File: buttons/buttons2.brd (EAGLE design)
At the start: 72 x 44 mm, 14 parts, among them U1 attiny2313

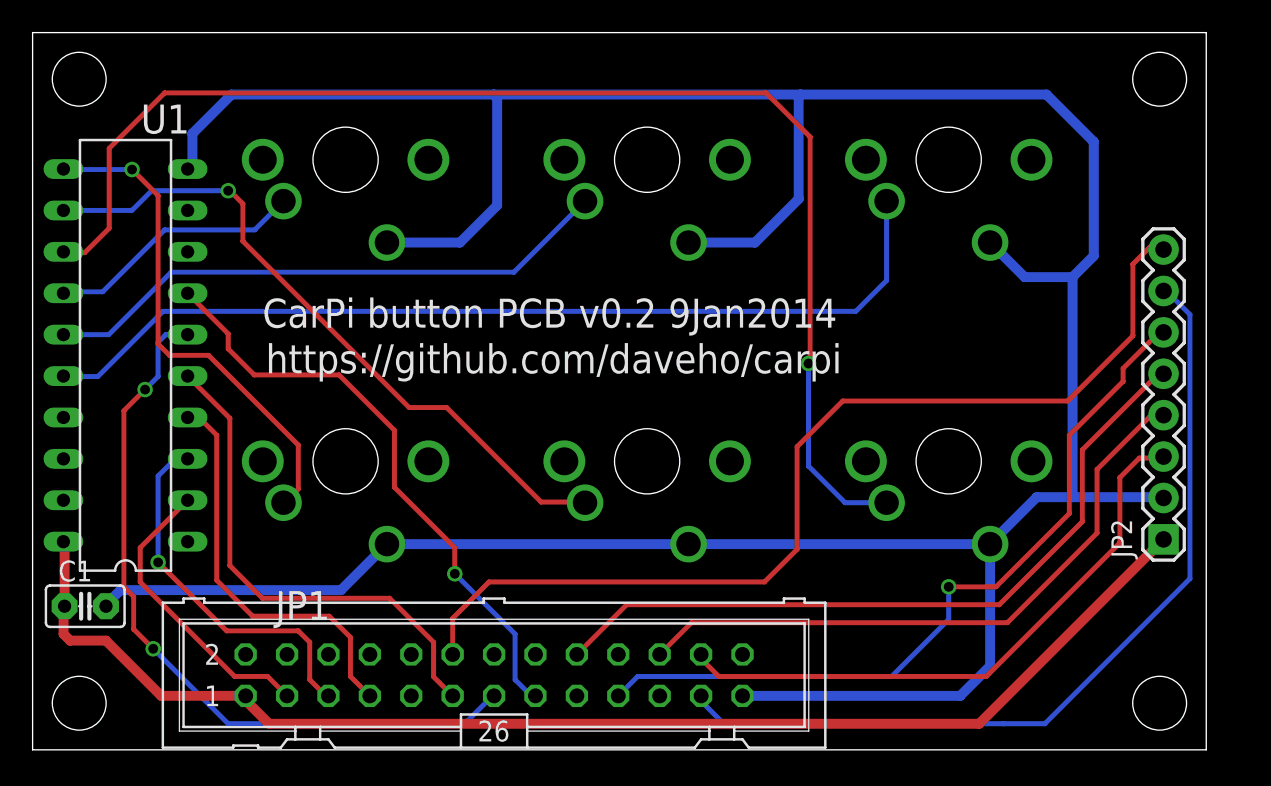
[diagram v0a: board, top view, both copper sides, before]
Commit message: making everything fit for Cherry MX keyswitches
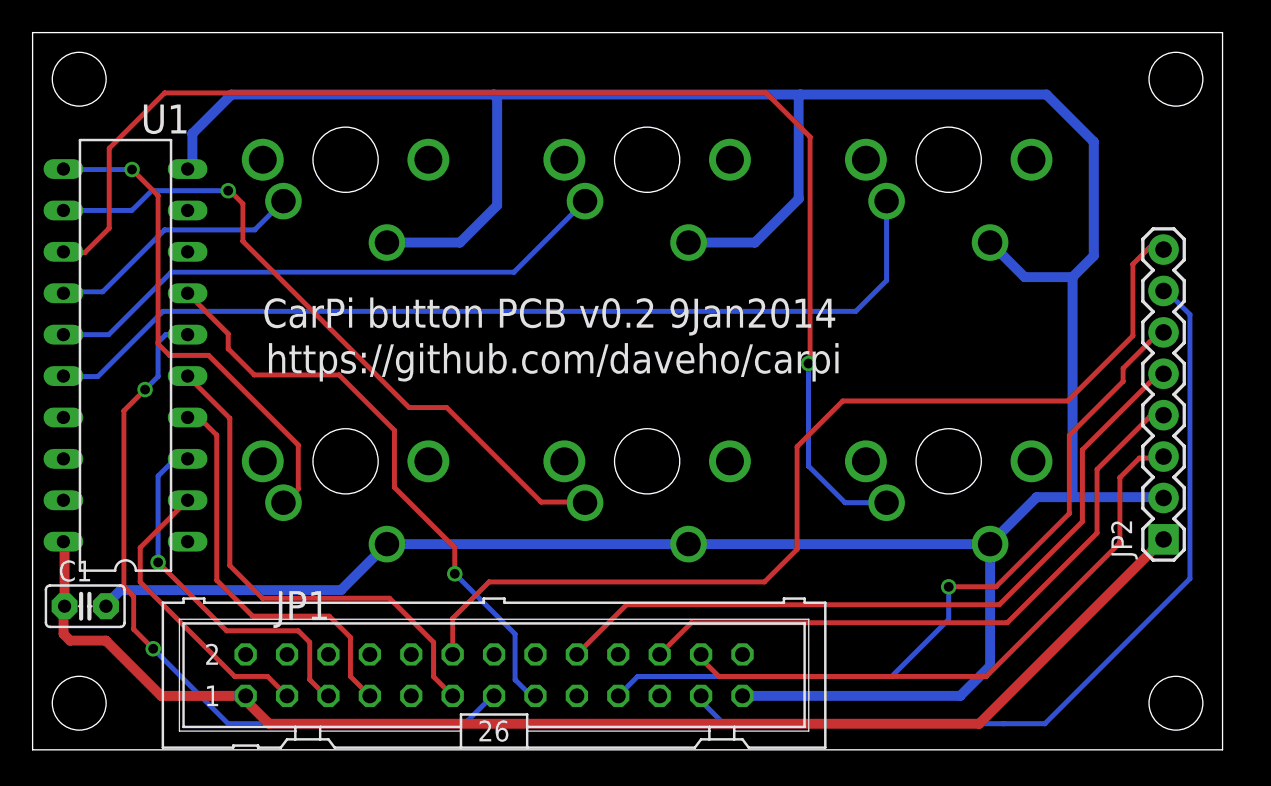
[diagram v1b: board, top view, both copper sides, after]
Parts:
- moved STANDOFF1 1.00 mm to (70.1, 2.86)
- moved STANDOFF3 1.00 mm to (70.1, 41.1)
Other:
- board size 72 x 44 mm -> 73 x 44 mm
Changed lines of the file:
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@@
 <board>
 <plain>
-<wire x1="0" y1="0" x2="72" y2="0" width="0" layer="20"/>
-<wire x1="72" y1="0" x2="72" y2="44" width="0" layer="20"/>
-<wire x1="72" y1="44" x2="0" y2="44" width="0" layer="20"/>
+<wire x1="0" y1="0" x2="73" y2="0" width="0" layer="20"/>
+<wire x1="73" y1="0" x2="73" y2="44" width="0" layer="20"/>
+<wire x1="73" y1="44" x2="0" y2="44" width="0" layer="20"/>
 <wire x1="0" y1="44" x2="0" y2="0" width="0" layer="20"/>
 <text x="14.1" y="25.9" size="1.778" layer="21" font="vector">CarPi button PCB v0.2 9Jan2014</text>
@@
 <attribute name="VALUE" x="0.679" y="6.016" size="1.27" layer="27" font="vector" ratio="10"/>
 </element>
-<element name="STANDOFF1" library="SparkFun-Electromechanical" package="STAND-OFF" value="STAND-OFF" x="69.14" y="2.86"/>
+<element name="STANDOFF1" library="SparkFun-Electromechanical" package="STAND-OFF" value="STAND-OFF" x="70.14" y="2.86"/>
 <element name="STANDOFF2" library="SparkFun-Electromechanical" package="STAND-OFF" value="STAND-OFF" x="2.86" y="2.86"/>
-<element name="STANDOFF3" library="SparkFun-Electromechanical" package="STAND-OFF" value="STAND-OFF" x="69.14" y="41.14"/>
+<element name="STANDOFF3" library="SparkFun-Electromechanical" package="STAND-OFF" value="STAND-OFF" x="70.14" y="41.14"/>
 <element name="STANDOFF4" library="SparkFun-Electromechanical" package="STAND-OFF" value="STAND-OFF" x="2.86" y="41.14"/>
 <element name="S1" library="cherrymx" package="CHERRY-MX-I" value="CHERRY-MX-I" x="19.2" y="17.7" rot="MR180"/>

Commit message: allow 19mm H/V between switch centers
The keycaps are 18mm x 18mm, so hopefull this is enough
room.
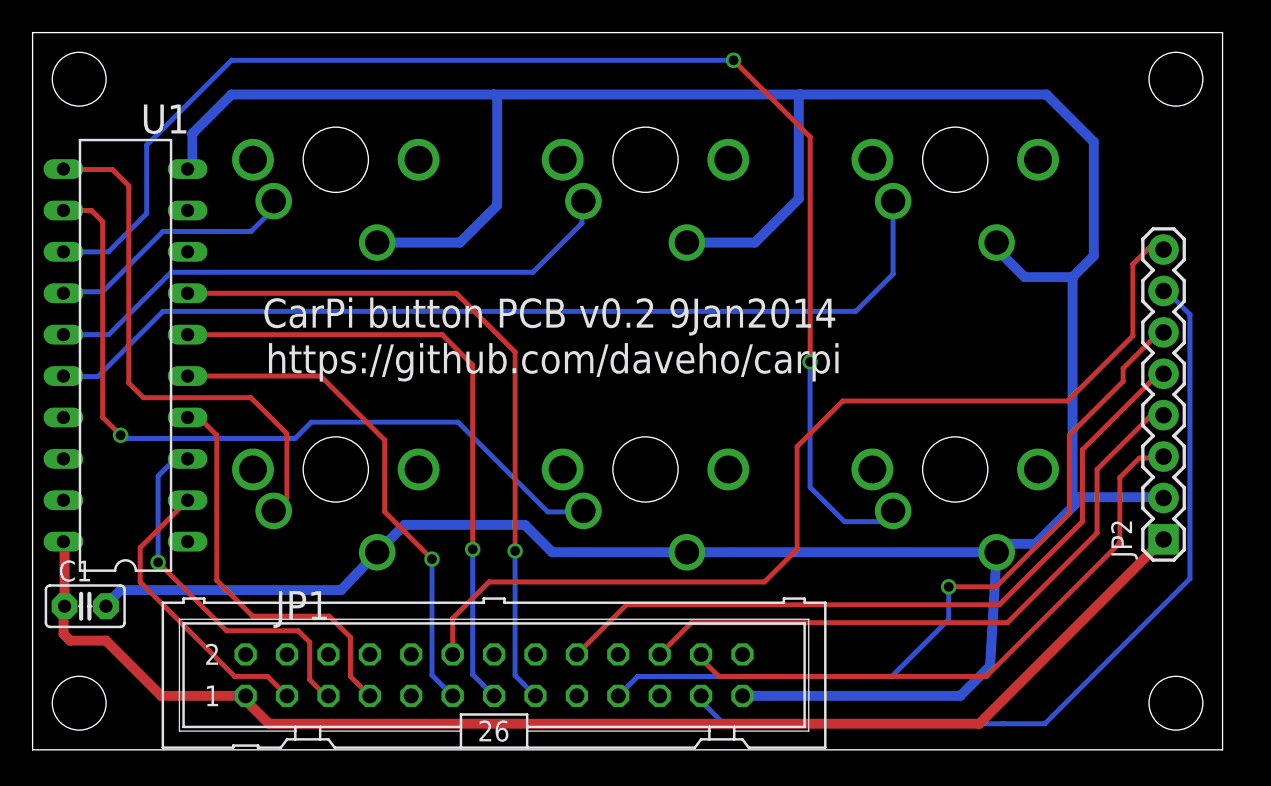
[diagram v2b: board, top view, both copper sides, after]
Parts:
- moved S1 0.78 mm to (18.6, 17.2)
- moved S3 0.64 mm to (56.6, 17.2)
- moved S4 0.60 mm to (18.6, 36.2)
- moved S2 0.51 mm to (37.6, 17.2)
- moved S6 0.40 mm to (56.6, 36.2)
- moved S5 0.10 mm to (37.6, 36.2)
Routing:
- net BUTTON5: track 45.9 -> 39.1 mm, vias 2 -> 1
- net BUTTON6: track 36.7 -> 43.2 mm
- net N$5: track 42.0 -> 47.4 mm
- net N$4: track 79.7 -> 82.8 mm, vias 1 -> 2
- net GND: track 208.3 -> 211.4 mm
- net N$6: track 30.7 -> 32.6 mm, vias 1 -> 0
- net N$2: track 35.4 -> 36.0 mm
- net BUTTON4: track 30.9 -> 31.1 mm, vias 0 -> 1

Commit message: various layout tweaks, improved clearances, etc.
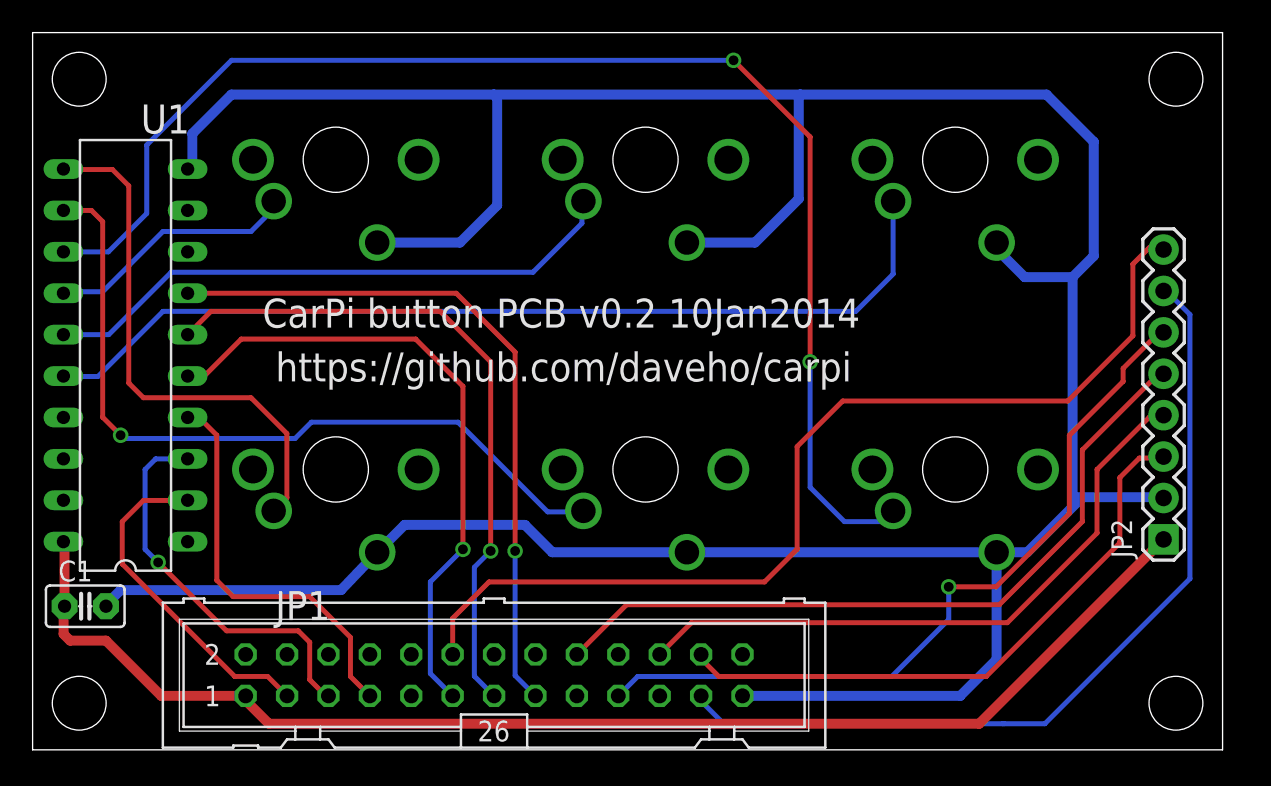
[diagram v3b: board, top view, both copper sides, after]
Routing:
- net BUTTON4: track 31.1 -> 39.4 mm
- net BUTTON5: track 39.1 -> 41.9 mm
- net BUTTON1: track 18.1 -> 20.6 mm
- net BUTTON2: track 22.7 -> 24.1 mm
- net GND: track 211.4 -> 210.7 mm
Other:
- board text added: "CarPi button PCB v0.2 10Jan2014"
- board text removed: "CarPi button PCB v0.2 9Jan2014"
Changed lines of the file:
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@@
 <wire x1="73" y1="44" x2="0" y2="44" width="0" layer="20"/>
 <wire x1="0" y1="44" x2="0" y2="0" width="0" layer="20"/>
-<text x="14.1" y="25.9" size="1.778" layer="21" font="vector">CarPi button PCB v0.2 9Jan2014</text>
-<text x="14.3" y="23.1" size="1.778" layer="21" font="vector">https://github.com/daveho/carpi</text>
+<text x="14.1" y="25.9" size="1.778" layer="21" font="vector">CarPi button PCB v0.2 10Jan2014</text>
+<text x="14.9" y="22.6" size="1.778" layer="21" font="vector">https://github.com/daveho/carpi</text>
 </plain>
 <attributes>
@@
 <contactref element="U1" pad="10"/>
 <contactref element="U1" pad="10"/>
-<wire x1="58.74" y1="5.14" x2="59.14" y2="12.12" width="0.6096" layer="16"/>
-<wire x1="59.14" y1="12.12" x2="58.74" y2="12.64" width="0.6096" layer="16"/>
 <wire x1="63.8" y1="15.5" x2="64.4" y2="15.5" width="0.6096" layer="16"/>
 <wire x1="64.4" y1="15.5" x2="69.33" y2="15.5" width="0.6096" layer="16"/>
@@
 <wire x1="9.8" y1="37.8" x2="12.2" y2="40.2" width="0.6096" layer="16"/>
 <wire x1="43.55" y1="3.31" x2="56.91" y2="3.31" width="0.6096" layer="16"/>
-<wire x1="56.91" y1="3.31" x2="58.74" y2="5.14" width="0.6096" layer="16"/>
+<wire x1="56.91" y1="3.31" x2="59.14" y2="5.54" width="0.6096" layer="16"/>
 <wire x1="12.2" y1="40.2" x2="28.3" y2="40.2" width="0.6096" layer="16"/>
 <wire x1="28.3" y1="40.2" x2="47.1" y2="40.2" width="0.6096" layer="16"/>
@@
 <wire x1="28.5" y1="33.4" x2="28.5" y2="40" width="0.6096" layer="16"/>
 <wire x1="28.5" y1="40" x2="28.3" y2="40.2" width="0.6096" layer="16"/>
-<wire x1="58.74" y1="12.64" x2="61.54" y2="12.64" width="0.6096" layer="16"/>
-<wire x1="61.54" y1="12.64" x2="64.4" y2="15.5" width="0.6096" layer="16"/>
+<wire x1="61.02" y1="12.12" x2="64.4" y2="15.5" width="0.6096" layer="16"/>
 <wire x1="59.14" y1="31.12" x2="58.94" y2="30.92" width="0.6096" layer="16"/>
 <wire x1="58.94" y1="30.92" x2="60.86" y2="29" width="0.6096" layer="16"/>
@@
 <wire x1="30.2" y1="13.8" x2="31.88" y2="12.12" width="0.6096" layer="16"/>
 <wire x1="31.88" y1="12.12" x2="40.14" y2="12.12" width="0.6096" layer="16"/>
+<wire x1="59.14" y1="12.12" x2="59.14" y2="5.54" width="0.6096" layer="16"/>
+<wire x1="59.14" y1="12.12" x2="61.02" y2="12.12" width="0.6096" layer="16"/>
 </signal>
 <signal name="N$1">
@@
 <contactref element="U1" pad="2"/>
 <wire x1="15.61" y1="3.31" x2="14.42" y2="4.5" width="0.3048" layer="1"/>
-<wire x1="6.6" y1="12.4" x2="9.51" y2="15.31" width="0.3048" layer="1"/>
-<wire x1="6.6" y1="12.4" x2="6.6" y2="10.3" width="0.3048" layer="1"/>
-<wire x1="6.6" y1="10.3" x2="12.4" y2="4.5" width="0.3048" layer="1"/>
+<wire x1="5.5" y1="11.4" x2="12.4" y2="4.5" width="0.3048" layer="1"/>
 <wire x1="12.4" y1="4.5" x2="14.42" y2="4.5" width="0.3048" layer="1"/>
+<wire x1="5.5" y1="11.4" x2="5.5" y2="14" width="0.3048" layer="1"/>
+<wire x1="5.5" y1="14" x2="6.8" y2="15.3" width="0.3048" layer="1"/>
+<wire x1="6.8" y1="15.3" x2="9.5" y2="15.3" width="0.3048" layer="1"/>
+<wire x1="9.5" y1="15.3" x2="9.51" y2="15.31" width="0.3048" layer="1"/>
 </signal>
 <signal name="BUTTON2">
@@
 <wire x1="11.9" y1="7.3" x2="7.7" y2="11.5" width="0.3048" layer="1"/>
 <via x="7.7" y="11.5" extent="1-16" drill="0.6"/>
-<wire x1="7.7" y1="11.5" x2="7.7" y2="16.8" width="0.3048" layer="16"/>
-<wire x1="7.7" y1="16.8" x2="8.7" y2="17.8" width="0.3048" layer="16"/>
-<wire x1="8.7" y1="17.8" x2="9.46" y2="17.8" width="0.3048" layer="16"/>
-<wire x1="9.46" y1="17.8" x2="9.51" y2="17.85" width="0.3048" layer="16"/>
+<wire x1="9.51" y1="17.85" x2="7.55" y2="17.85" width="0.3048" layer="16"/>
+<wire x1="7.55" y1="17.85" x2="6.9" y2="17.2" width="0.3048" layer="16"/>
+<wire x1="6.9" y1="17.2" x2="6.9" y2="12.3" width="0.3048" layer="16"/>
+<wire x1="6.9" y1="12.3" x2="7.7" y2="11.5" width="0.3048" layer="16"/>
 </signal>
 <signal name="BUTTON3">
@@
 <wire x1="20.69" y1="3.31" x2="19.5" y2="4.5" width="0.3048" layer="1"/>
 <wire x1="19.5" y1="4.5" x2="19.5" y2="6.9" width="0.3048" layer="1"/>
-<wire x1="19.5" y1="6.9" x2="18.2" y2="8.2" width="0.3048" layer="1"/>
-<wire x1="18.2" y1="8.2" x2="13.5" y2="8.2" width="0.3048" layer="1"/>
-<wire x1="13.5" y1="8.2" x2="11.3" y2="10.4" width="0.3048" layer="1"/>
+<wire x1="19.5" y1="6.9" x2="17" y2="9.4" width="0.3048" layer="1"/>
 <wire x1="11.3" y1="19.3" x2="10.2" y2="20.4" width="0.3048" layer="1"/>
 <wire x1="10.2" y1="20.4" x2="9.52" y2="20.4" width="0.3048" layer="1"/>
 <wire x1="9.52" y1="20.4" x2="9.51" y2="20.39" width="0.3048" layer="1"/>
 <wire x1="11.3" y1="10.4" x2="11.3" y2="19.3" width="0.3048" layer="1"/>
+<wire x1="17" y1="9.4" x2="12.3" y2="9.4" width="0.3048" layer="1"/>
+<wire x1="12.3" y1="9.4" x2="11.3" y2="10.4" width="0.3048" layer="1"/>
 </signal>
 <signal name="BUTTON4">
 <contactref element="JP1" pad="11"/>
 <contactref element="U1" pad="5"/>
-<wire x1="9.51" y1="22.93" x2="17.67" y2="22.93" width="0.3048" layer="1"/>
-<wire x1="17.67" y1="22.93" x2="21.6" y2="19" width="0.3048" layer="1"/>
-<wire x1="21.6" y1="19" x2="21.6" y2="14.6" width="0.3048" layer="1"/>
-<wire x1="21.6" y1="14.6" x2="24.5" y2="11.7" width="0.3048" layer="1"/>
-<wire x1="25.77" y1="3.31" x2="24.5" y2="4.58" width="0.3048" layer="16"/>
-<wire x1="24.5" y1="4.58" x2="24.5" y2="11.7" width="0.3048" layer="16"/>
-<via x="24.5" y="11.7" extent="1-16" drill="0.6"/>
+<wire x1="25.77" y1="3.31" x2="24.4" y2="4.68" width="0.3048" layer="16"/>
+<wire x1="24.4" y1="4.68" x2="24.4" y2="10.3" width="0.3048" layer="16"/>
+<wire x1="24.4" y1="10.3" x2="26.4" y2="12.3" width="0.3048" layer="16"/>
+<via x="26.4" y="12.3" extent="1-16" drill="0.6"/>
+<wire x1="9.51" y1="22.93" x2="10.53" y2="22.93" width="0.3048" layer="1"/>
+<wire x1="10.53" y1="22.93" x2="12.8" y2="25.2" width="0.3048" layer="1"/>
+<wire x1="12.8" y1="25.2" x2="23.5" y2="25.2" width="0.3048" layer="1"/>
+<wire x1="23.5" y1="25.2" x2="26.4" y2="22.3" width="0.3048" layer="1"/>
+<wire x1="26.4" y1="22.3" x2="26.4" y2="12.3" width="0.3048" layer="1"/>
 </signal>
 <signal name="BUTTON5">
 <contactref element="JP1" pad="13"/>
 <contactref element="U1" pad="6"/>
-<wire x1="9.51" y1="25.47" x2="25.13" y2="25.47" width="0.3048" layer="1"/>
-<wire x1="28.31" y1="3.31" x2="27" y2="4.62" width="0.3048" layer="16"/>
-<wire x1="27" y1="4.62" x2="27" y2="12.3" width="0.3048" layer="16"/>
-<via x="27" y="12.3" extent="1-16" drill="0.6"/>
-<wire x1="25.13" y1="25.47" x2="27" y2="23.6" width="0.3048" layer="1"/>
-<wire x1="27" y1="23.6" x2="27" y2="12.3" width="0.3048" layer="1"/>
+<wire x1="28.31" y1="3.31" x2="27.1" y2="4.52" width="0.3048" layer="16"/>
+<wire x1="27.1" y1="4.52" x2="27.1" y2="11.2" width="0.3048" layer="16"/>
+<wire x1="27.1" y1="11.2" x2="28.1" y2="12.2" width="0.3048" layer="16"/>
+<via x="28.1" y="12.2" extent="1-16" drill="0.6"/>
+<wire x1="9.51" y1="25.47" x2="10.94" y2="26.9" width="0.3048" layer="1"/>
+<wire x1="10.94" y1="26.9" x2="25" y2="26.9" width="0.3048" layer="1"/>
+<wire x1="25" y1="26.9" x2="28.1" y2="23.8" width="0.3048" layer="1"/>
+<wire x1="28.1" y1="23.8" x2="28.1" y2="12.2" width="0.3048" layer="1"/>
 </signal>
 <signal name="BUTTON6">

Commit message: more minor routing improvements
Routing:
- net MOSI: track 47.1 -> 48.1 mm
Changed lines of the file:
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@@
 <contactref element="JP2" pad="6"/>
 <contactref element="JP1" pad="19"/>
-<wire x1="69.38" y1="25.61" x2="69.11" y2="25.61" width="0.3048" layer="1"/>
-<wire x1="69.11" y1="25.61" x2="66.9" y2="23.4" width="0.3048" layer="1"/>
-<wire x1="66.9" y1="23.4" x2="66.9" y2="22.6" width="0.3048" layer="1"/>
-<wire x1="66.9" y1="22.6" x2="63.6" y2="19.3" width="0.3048" layer="1"/>
-<wire x1="63.6" y1="19.3" x2="63.6" y2="14.5" width="0.3048" layer="1"/>
-<wire x1="63.6" y1="14.5" x2="59.1" y2="10" width="0.3048" layer="1"/>
-<wire x1="59.1" y1="10" x2="56.2" y2="10" width="0.3048" layer="1"/>
-<via x="56.2" y="10" extent="1-16" drill="0.6"/>
-<wire x1="56.2" y1="10" x2="56.2" y2="8" width="0.3048" layer="16"/>
-<wire x1="56.2" y1="8" x2="52.7" y2="4.5" width="0.3048" layer="16"/>
-<wire x1="52.7" y1="4.5" x2="37.12" y2="4.5" width="0.3048" layer="16"/>
-<wire x1="37.12" y1="4.5" x2="35.93" y2="3.31" width="0.3048" layer="16"/>
+<wire x1="69.38" y1="25.61" x2="63.97" y2="20.2" width="0.3048" layer="1"/>
+<wire x1="63.97" y1="20.2" x2="50.7" y2="20.2" width="0.3048" layer="1"/>
+<wire x1="50.7" y1="20.2" x2="48.4" y2="17.9" width="0.3048" layer="1"/>
+<wire x1="48.4" y1="17.9" x2="48.4" y2="10.8" width="0.3048" layer="1"/>
+<via x="48.4" y="10.8" extent="1-16" drill="0.6"/>
+<wire x1="48.4" y1="10.8" x2="45.6" y2="8" width="0.3048" layer="16"/>
+<wire x1="45.6" y1="8" x2="38.5" y2="8" width="0.3048" layer="16"/>
+<wire x1="38.5" y1="8" x2="37.1" y2="6.6" width="0.3048" layer="16"/>
+<wire x1="37.1" y1="6.6" x2="37.1" y2="4.5" width="0.3048" layer="16"/>
+<wire x1="37.1" y1="4.5" x2="35.93" y2="3.33" width="0.3048" layer="16"/>
+<wire x1="35.93" y1="3.33" x2="35.93" y2="3.31" width="0.3048" layer="16"/>
 </signal>
 <signal name="SCK">

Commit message: more routing tweaks
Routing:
- net N$5: track 47.4 -> 48.8 mm
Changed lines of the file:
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@@
 <via x="5.4" y="19.3" extent="1-16" drill="0.6"/>
 <wire x1="5.4" y1="19.3" x2="5.6" y2="19.1" width="0.3048" layer="16"/>
-<wire x1="5.6" y1="19.1" x2="16.1" y2="19.1" width="0.3048" layer="16"/>
-<wire x1="16.1" y1="19.1" x2="17.1" y2="20.1" width="0.3048" layer="16"/>
-<wire x1="17.1" y1="20.1" x2="26.1" y2="20.1" width="0.3048" layer="16"/>
-<wire x1="26.1" y1="20.1" x2="31.6" y2="14.6" width="0.3048" layer="16"/>
+<wire x1="5.6" y1="19.1" x2="11.3" y2="19.1" width="0.3048" layer="16"/>
+<wire x1="11.3" y1="19.1" x2="13.1" y2="19.1" width="0" layer="19" extent="1-16"/>
+<wire x1="24.5" y1="21.7" x2="31.6" y2="14.6" width="0.3048" layer="16"/>
 <wire x1="31.6" y1="14.6" x2="33.73" y2="14.6" width="0.3048" layer="16"/>
 <wire x1="33.73" y1="14.6" x2="33.79" y2="14.66" width="0.3048" layer="16"/>
+<wire x1="24.5" y1="21.7" x2="13.9" y2="21.7" width="0.3048" layer="16"/>
+<wire x1="13.9" y1="21.7" x2="11.3" y2="19.1" width="0.3048" layer="16"/>
 </signal>
 <signal name="N$6">
